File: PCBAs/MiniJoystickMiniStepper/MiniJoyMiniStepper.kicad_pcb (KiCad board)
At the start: 2 copper layers, 88.9 x 142.2 mm, 94 parts, among them J0 STEPPER_UNI_5P, J1 STEPPER_UNI_5P, J10 TH_0.1_1x1, J100 TH_0.1_1x1, J101 TH_0.1_1x1, J102 TH_0.1_1x1, J103 TH_0.1_1x1, J104 TH_0.1_1x1, J105 TH_0.1_1x1, J107 TH_0.1_1x1, J11 TH_0.1_1x1, J12 TH_0.1_1x1, J13 TH_0.1_1x1, J14 TH_0.1_1x1, J15 TH_0.1_1x1, J16 TH_0.1_1x1, J2 STEPPER_UNI_5P, J3 STEPPER_UNI_5P, J4 STEPPER_UNI_5P, J5 STEPPER_UNI_5P, J6 STEPPER_UNI_5P, J7 STEPPER_UNI_5P, J8 TH_0.1_1x1, J9 TH_0.1_1x1, U1 MCP3008T-I/SL, U10 ULN2803, U11 STM32F103C8T6_BLUE_PILL, U2 OLED_128x32_I2C, U3 CD74HC595, U4 CD74HC595, U5 CD74HC595, U6 CD74HC595, U7 ULN2803, U8 ULN2803, U9 ULN2803

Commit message: PCB mid-route
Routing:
- net /!MOTOR_SCLR: track 81.3 -> 211.3 mm, vias 5 -> 13
- net Net-(J_MOTOR_DATA_OUT1-Pad1): track 0.00 -> 49.7 mm, vias 0 -> 2
- net Net-(U4-Pad9): track 0.00 -> 43.6 mm, vias 0 -> 2
- net Net-(U4-Pad14): track 0.00 -> 42.7 mm, vias 0 -> 2
- net /MOTOR_CLK_OUT: track 195.1 -> 196.1 mm
- net /MOTOR_CLK_SHIFT: track 188.3 -> 189.0 mm

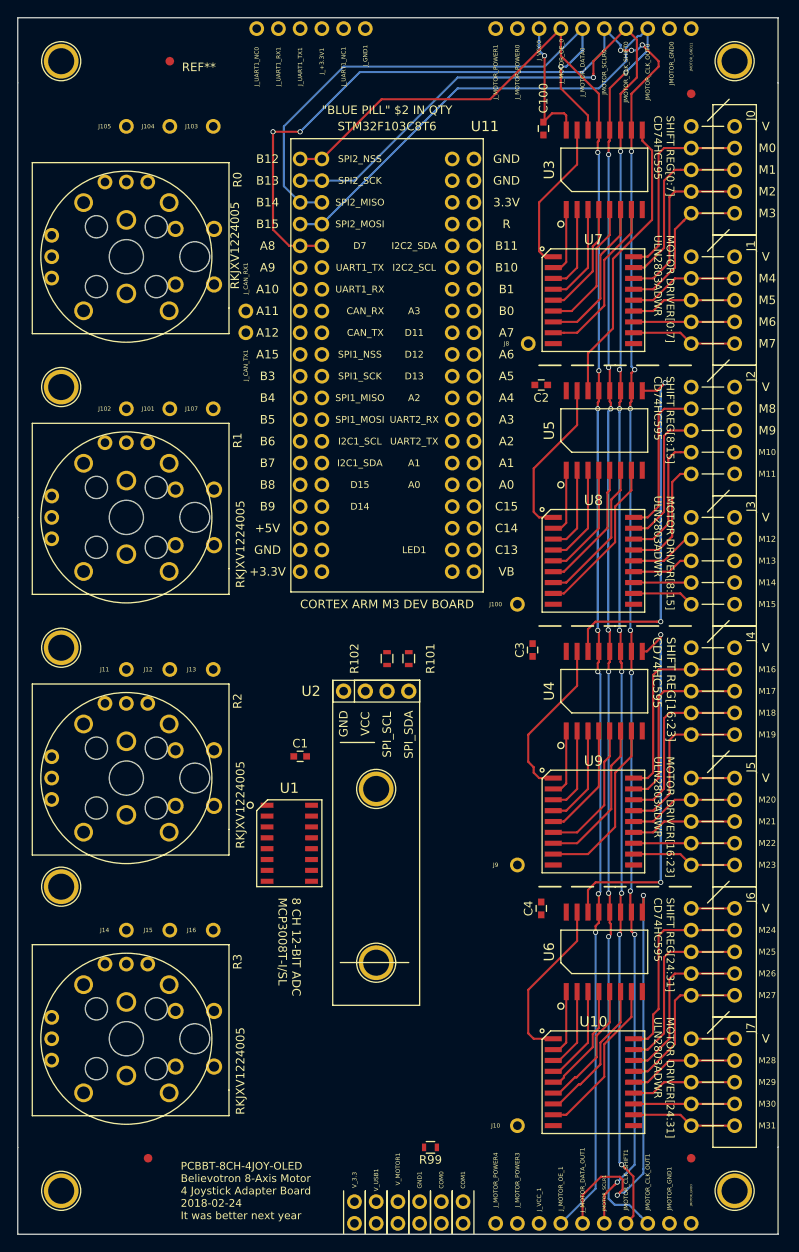
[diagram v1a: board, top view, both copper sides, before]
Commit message: PCB Midroute: Motor Driver + Shift Register routed.
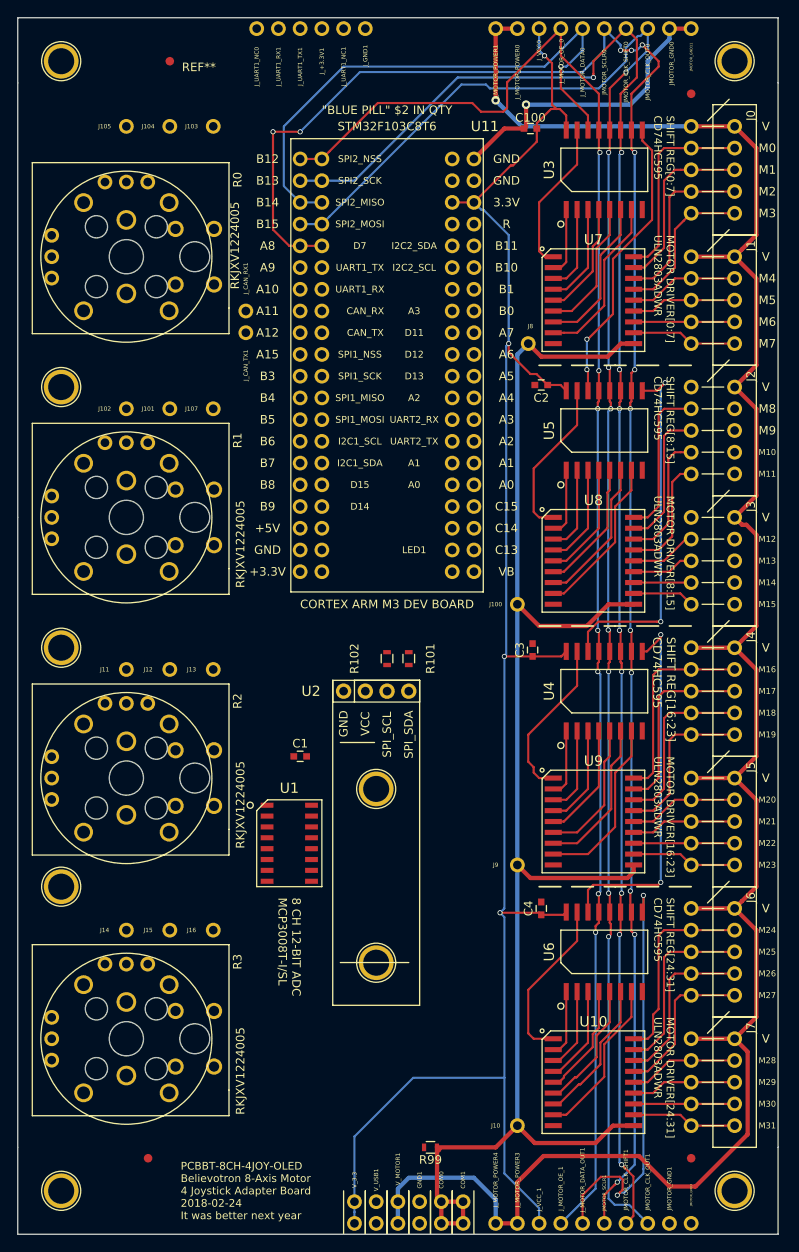
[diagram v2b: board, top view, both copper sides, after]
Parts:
- moved C100 1.52 mm to (161.5, 30.7), turned to 180 degrees
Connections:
- J_MOTOR_POWER0 pad 1: Net-(J_MOTOR_POWER0-Pad1) -> /MOTOR_POWER
- J_MOTOR_POWER1 pad 1: Net-(J_MOTOR_POWER1-Pad1) -> /MOTOR_POWER
- J_MOTOR_POWER3 pad 1: Net-(J_MOTOR_POWER3-Pad1) -> /MOTOR_POWER
- J_MOTOR_POWER4 pad 1: Net-(J_MOTOR_POWER4-Pad1) -> /MOTOR_POWER
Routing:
- net /MOTOR_POWER: track 15.2 -> 258.5 mm, vias 0 -> 1
- net +3V3: track 16.0 -> 210.5 mm, vias 1 -> 4
- net /COM: track 0.00 -> 179.0 mm
- net GND: track 0.00 -> 35.7 mm, vias 0 -> 1
- net /!MOTOR_OE: track 180.7 -> 183.3 mm
- net Net-(U3-Pad9): track 34.1 -> 34.2 mm, vias 0 -> 2

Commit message: PCB Mid route
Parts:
- turned R101 to 270 degrees
- turned R102 to 270 degrees
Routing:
- net /JOY3_SW: track 0.00 -> 106.0 mm
- net /SPI1_CS: track 0.00 -> 73.8 mm, vias 0 -> 1
- net /SPI1_SCK: track 0.00 -> 62.5 mm, vias 0 -> 1
- net /SPI1_MISO: track 0.00 -> 59.4 mm, vias 0 -> 1
- net /SPI1_MOSI: track 0.00 -> 55.2 mm, vias 0 -> 1
- net /JOY2_AXIS0: track 0.00 -> 54.1 mm, vias 0 -> 1
- net +3V3: track 210.5 -> 262.9 mm
- net /I2C1_SCL: track 0.00 -> 46.9 mm
- net /JOY3_AXIS0: track 0.00 -> 42.4 mm
- net Net-(J_UART1_RX1-Pad1): track 0.00 -> 37.1 mm
- net /I2C1_SDA: track 0.00 -> 36.5 mm
- net /JOY2_AXIS1: track 0.00 -> 36.2 mm
- net Net-(J_UART1_TX1-Pad1): track 0.00 -> 35.4 mm
- net /JOY3_AXIS1: track 0.00 -> 20.5 mm
- net /!MOTOR_SCLR: track 211.3 -> 211.2 mm, vias 13 -> 12

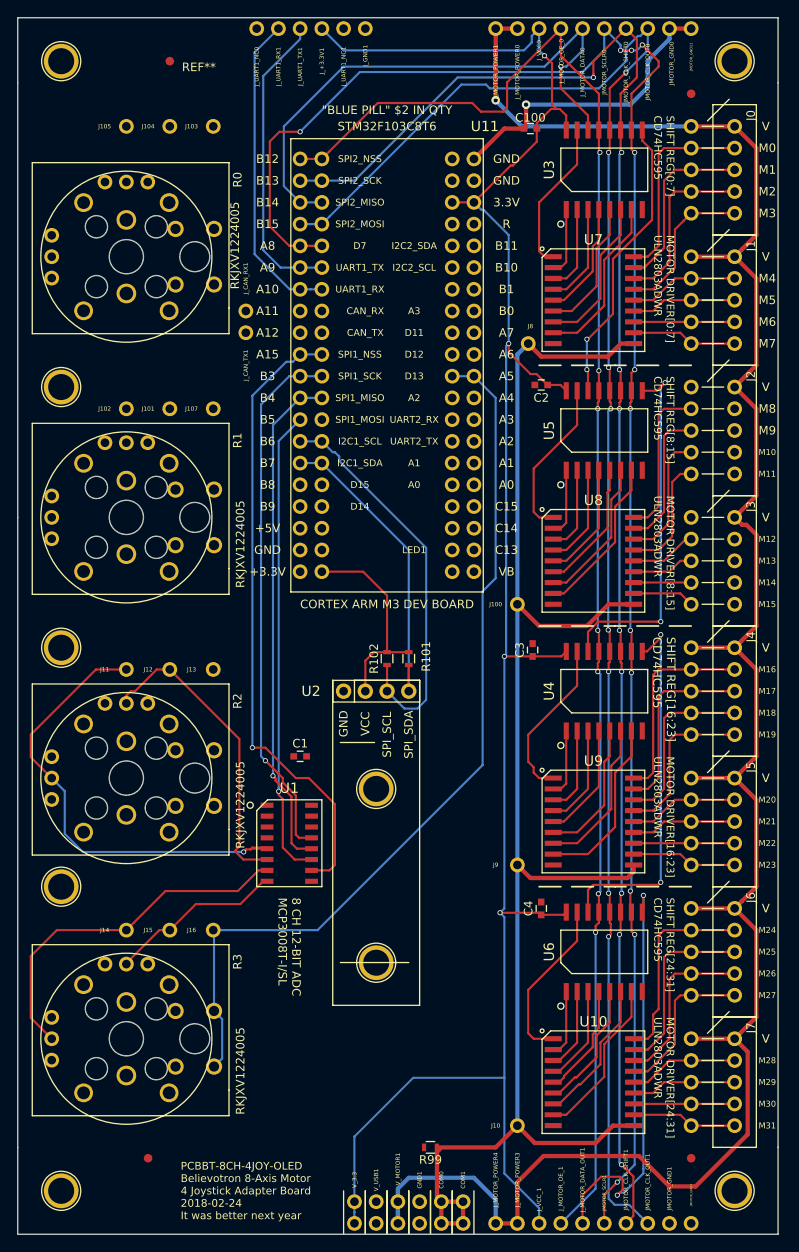
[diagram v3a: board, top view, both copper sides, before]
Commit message: PCB First route complete. Files not ready for fab.
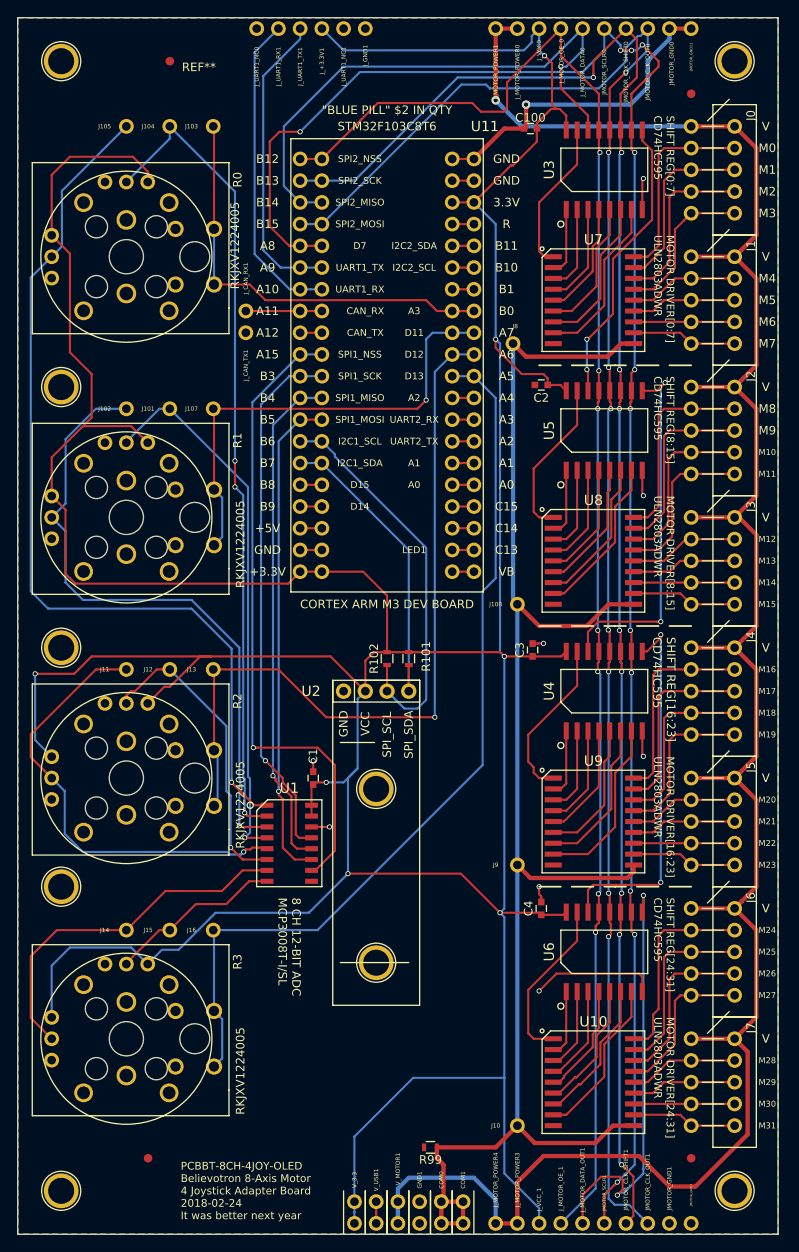
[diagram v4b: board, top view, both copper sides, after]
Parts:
- moved C1 2.96 mm to (136.1, 106.7), turned to 90 degrees
- moved J8 1.78 mm to (159.5, 55.9)
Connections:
- R0 pad J0-1: VCC -> +3V3
- R0 pad J1-1: VCC -> +3V3
- R1 pad J0-1: VCC -> +3V3
- R1 pad J1-1: VCC -> +3V3
- R2 pad J0-1: VCC -> +3V3
- R2 pad J1-1: VCC -> +3V3
- R3 pad J0-1: VCC -> +3V3
- R3 pad J1-1: VCC -> +3V3
- U1 pad 3: Net-(U1-Pad3) -> /JOY1_AXIS0
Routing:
- net +3V3: track 262.9 -> 540.1 mm, vias 4 -> 7
- net /JOY0_AXIS0: track 0.00 -> 106.1 mm, vias 0 -> 1
- net /JOY0_AXIS1: track 0.00 -> 95.3 mm, vias 0 -> 3
- net /JOY2_SW: track 0.00 -> 90.4 mm, vias 0 -> 1
- net /JOY1_AXIS0: track 0.00 -> 74.4 mm, vias 0 -> 1
- net /JOY1_AXIS1: track 0.00 -> 63.7 mm, vias 0 -> 1
- net /JOY1_SW: track 0.00 -> 55.1 mm, vias 0 -> 1
- net /JOY0_SW: track 0.00 -> 50.2 mm
- net GND: track 35.7 -> 74.4 mm, vias 1 -> 9
- net /MOTOR_POWER: track 258.5 -> 268.6 mm
- net Net-(J_CAN_RX1-Pad1): track 0.00 -> 8.89 mm
- net Net-(J2-Pad3): track 16.7 -> 21.8 mm
- net Net-(J3-Pad3): track 7.26 -> 12.3 mm
- net Net-(J3-Pad2): track 7.78 -> 12.9 mm
- net Net-(J3-Pad5): track 7.26 -> 12.3 mm
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- added copper zone on B.Cu, net GND
- added copper zone on F.Cu, net GND

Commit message: Generated Gerbers. Ready for fab!
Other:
- board text added: "PCBBT-8CH-4JOY-OLED Believotron 8-Axis Motor 4 Joystick Adapter Board 2018-03-19 It was better next year"
- board text removed: "PCBBT-8CH-4JOY-OLED Believotron 8-Axis Motor 4 Joystick Adapter Board 2018-02-24 It was better next year"
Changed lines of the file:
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@@
     (links 309)
     (no_connects 0)
-    (area 101.524999 17.704999 190.575001 160.095001)
+    (area 99.901904 14.635714 197.278096 163.164286)
     (thickness 1.6)
     (drawings 81)
@@
     (visible_elements 7FFFFFFF)
     (pcbplotparams
-      (layerselection 0x00030_80000001)
+      (layerselection 0x0103c_80000001)
       (usegerberextensions false)
       (excludeedgelayer true)
@@
       (outputformat 1)
       (mirror false)
-      (drillshape 1)
+      (drillshape 0)
       (scaleselection 1)
-      (outputdirectory ""))
+      (outputdirectory Output/PCBBT-8CH-4JOY-OLED_Gerbers_2018-03-19/))
   )
   (net 0 "")
@@
   (gr_line (start 101.6 160.02) (end 190.5 160.02) (layer Edge.Cuts) (width 0.15))
   (gr_line (start 101.6 76.2) (end 101.6 25.4) (layer Edge.Cuts) (width 0.15))
-  (gr_text "PCBBT-8CH-4JOY-OLED\nBelievotron 8-Axis Motor \n4 Joystick Adapter Board\n2018-02-24\nIt was better next year" (at 120.65 154.94) (layer F.SilkS)
+  (gr_text "PCBBT-8CH-4JOY-OLED\nBelievotron 8-Axis Motor \n4 Joystick Adapter Board\n2018-03-19\nIt was better next year" (at 120.65 154.94) (layer F.SilkS)
     (effects (font (size 0.9 0.9) (thickness 0.1875)) (justify left))
   )
